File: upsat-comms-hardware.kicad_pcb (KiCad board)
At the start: 4 copper layers, 92.5 x 92.5 mm, 290 parts, among them J1 SMA, J2 SMA, P1 SWD, P2 OBC, P3 CONN_02X03, U1 TXCO_TG_5021CG, U10 CC1120, U12 ADT7420, U14 OPA320, U16 RF5110G, U18 FA_128_, U2 TPS79930, U3 FA_128_, U4 CC1120, U5 STM32F407VG, U6 TXCO_TG_5021CG, U8 TPS79930, Y1 Crystal, Y2 Crystal

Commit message: Restructuring libraries.
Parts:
- moved R72 0.05 mm to (132.4, 102.0)
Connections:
- P2 pad 6: Net-(P2-Pad6) -> (no net)
- U1 pad 1: Net-(U1-Pad1) -> (no net)
- U10 pad 16: Net-(U10-Pad16) -> (no net)
- U12 pad 10: Net-(U12-Pad10) -> (no net)
- U12 pad 13: Net-(U12-Pad13) -> (no net)
- U12 pad 14: Net-(U12-Pad14) -> (no net)
- U12 pad 15: Net-(U12-Pad15) -> (no net)
- U12 pad 16: Net-(U12-Pad16) -> (no net)
- U12 pad 5: Net-(U12-Pad5) -> (no net)
- U12 pad 6: Net-(U12-Pad6) -> (no net)
- U12 pad 7: Net-(U12-Pad7) -> (no net)
- U12 pad 8: Net-(U12-Pad8) -> (no net)
- U12 pad 9: Net-(U12-Pad9) -> (no net)
- U16 pad 13: Net-(U16-Pad13) -> (no net)
- U16 pad 7: Net-(U16-Pad7) -> (no net)
- U4 pad 16: Net-(U4-Pad16) -> (no net)
- U5 pad 1: Net-(U5-Pad1) -> (no net)
- U5 pad 15: Net-(U5-Pad15) -> (no net)
- U5 pad 16: Net-(U5-Pad16) -> (no net)
- U5 pad 17: Net-(U5-Pad17) -> (no net)
- U5 pad 18: Net-(U5-Pad18) -> (no net)
- U5 pad 2: Net-(U5-Pad2) -> (no net)
- U5 pad 23: Net-(U5-Pad23) -> (no net)
- U5 pad 24: Net-(U5-Pad24) -> (no net)
- U5 pad 29: Net-(U5-Pad29) -> (no net)
- U5 pad 3: Net-(U5-Pad3) -> (no net)
- U5 pad 33: Net-(U5-Pad33) -> (no net)
- U5 pad 34: Net-(U5-Pad34) -> (no net)
- U5 pad 35: Net-(U5-Pad35) -> (no net)
- U5 pad 37: Net-(U5-Pad37) -> (no net)
- U5 pad 39: Net-(U5-Pad39) -> (no net)
- U5 pad 4: Net-(U5-Pad4) -> (no net)
- U5 pad 41: Net-(U5-Pad41) -> (no net)
- U5 pad 42: Net-(U5-Pad42) -> (no net)
- U5 pad 43: Net-(U5-Pad43) -> (no net)
- U5 pad 44: Net-(U5-Pad44) -> (no net)
- U5 pad 45: Net-(U5-Pad45) -> (no net)
- U5 pad 5: Net-(U5-Pad5) -> (no net)
- U5 pad 55: Net-(U5-Pad55) -> (no net)
- U5 pad 56: Net-(U5-Pad56) -> (no net)
- U5 pad 57: Net-(U5-Pad57) -> (no net)
- U5 pad 58: Net-(U5-Pad58) -> (no net)
- U5 pad 59: Net-(U5-Pad59) -> (no net)
- U5 pad 60: Net-(U5-Pad60) -> (no net)
- U5 pad 61: Net-(U5-Pad61) -> (no net)
- U5 pad 62: Net-(U5-Pad62) -> (no net)
- U5 pad 63: Net-(U5-Pad63) -> (no net)
- U5 pad 64: Net-(U5-Pad64) -> (no net)
- U5 pad 65: Net-(U5-Pad65) -> (no net)
- U5 pad 66: Net-(U5-Pad66) -> (no net)
- U5 pad 68: Net-(U5-Pad68) -> (no net)
- U5 pad 7: Net-(U5-Pad7) -> (no net)
- U5 pad 70: Net-(U5-Pad70) -> (no net)
- U5 pad 71: Net-(U5-Pad71) -> (no net)
- U5 pad 78: Net-(U5-Pad78) -> (no net)
- U5 pad 79: Net-(U5-Pad79) -> (no net)
- U5 pad 81: Net-(U5-Pad81) -> (no net)
- U5 pad 82: Net-(U5-Pad82) -> (no net)
- U5 pad 85: Net-(U5-Pad85) -> (no net)
- U5 pad 86: Net-(U5-Pad86) -> (no net)
- U5 pad 87: Net-(U5-Pad87) -> (no net)
- U5 pad 88: Net-(U5-Pad88) -> (no net)
- U5 pad 90: Net-(U5-Pad90) -> (no net)
- U5 pad 91: Net-(U5-Pad91) -> (no net)
- U5 pad 92: Net-(U5-Pad92) -> (no net)
- U5 pad 93: Net-(U5-Pad93) -> (no net)
- U5 pad 97: Net-(U5-Pad97) -> (no net)
- U5 pad 98: Net-(U5-Pad98) -> (no net)
- U6 pad 1: Net-(U6-Pad1) -> (no net)
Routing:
- net Net-(R72-Pad2): track 29.2 -> 24.5 mm
- net Net-(R73-Pad2): track 30.0 -> 26.3 mm
- net /I2C1_SDA: track 150.8 -> 149.4 mm
- net /I2C1_SCL: track 153.8 -> 152.7 mm
- net /DAC_OUT2: track 100.0 -> 98.9 mm
- net Net-(R70-Pad2): track 22.3 -> 22.9 mm

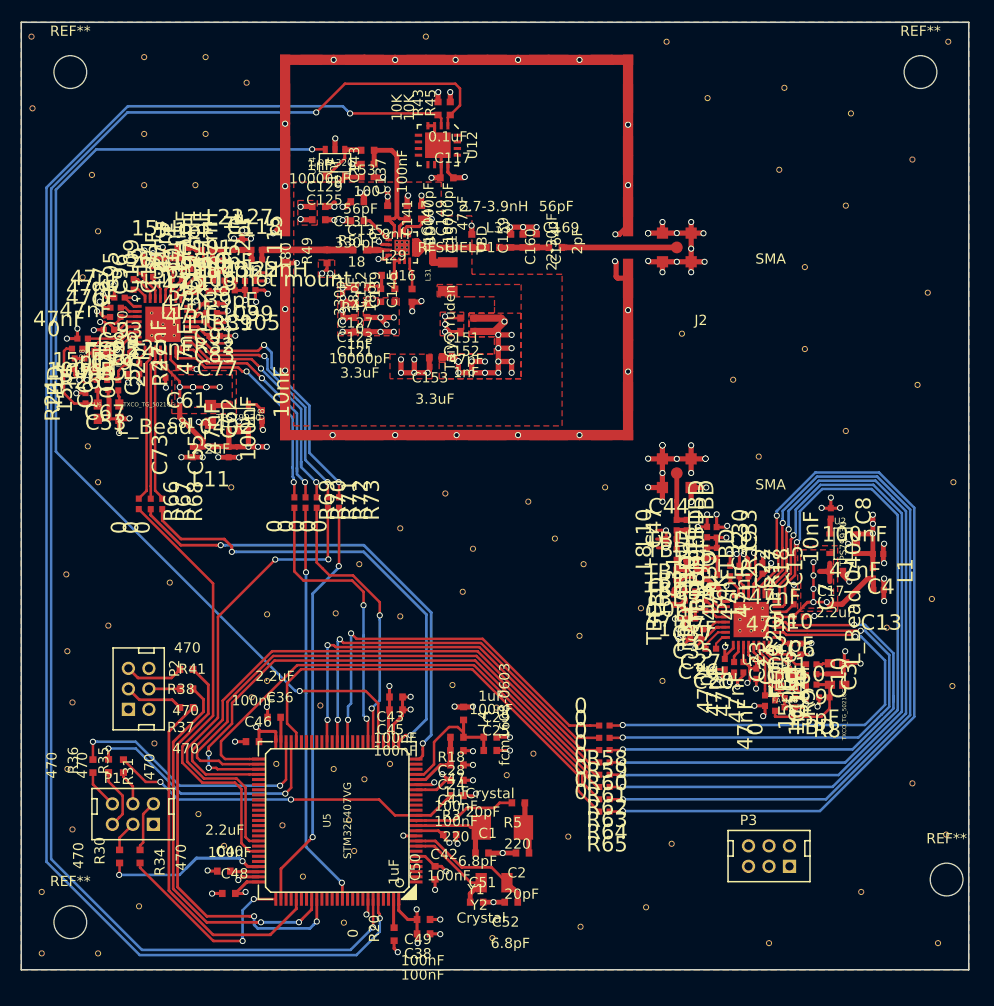
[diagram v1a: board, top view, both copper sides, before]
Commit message: Create silkscreen and reroute OBC Connector.
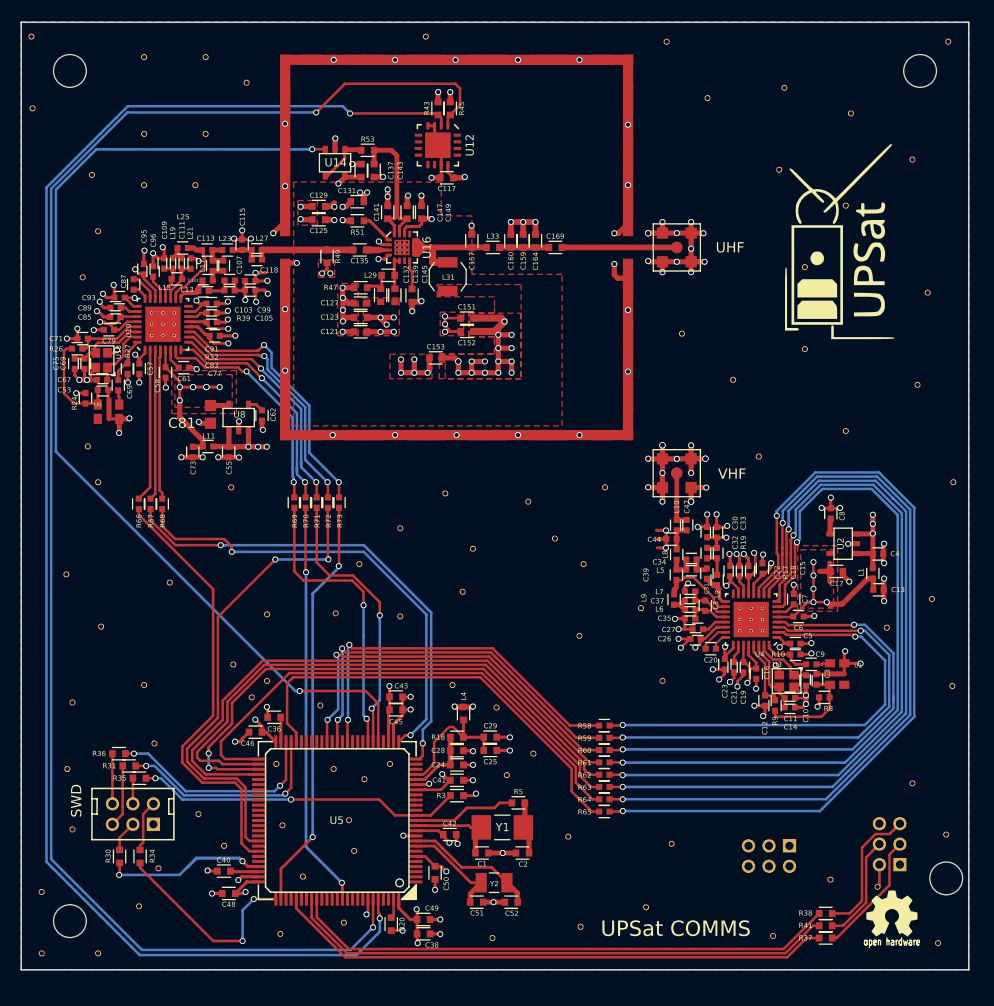
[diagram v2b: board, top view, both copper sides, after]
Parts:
- added G***: LOGO, libs:upsat-logo, F.Cu at (182.4, 76.0)
- added G***: LOGO, w_logo:Logo_silk_OSHW_6x6mm, F.Cu at (187.5, 141.6)
- added REF**: VIA-0.6mm, via:VIA-0.6mm, F.Cu at (127.8, 143.6)
- added REF**: VIA-0.6mm, via:VIA-0.6mm, F.Cu at (181.5, 138.3)
- added REF**: VIA-0.6mm, via:VIA-0.6mm, F.Cu at (123.2, 117.3)
- added REF**: VIA-0.6mm, via:VIA-0.6mm, F.Cu at (115.9, 137.2)
- EPS: renamed from P3; moved to B.Cu
- OBC: renamed from P2; moved to B.Cu
- RFSHIELD1: footprint libs:BMI-S-x06 -> BMI-S-x06:BMI-S-x06
- U18, U3: footprint w_crystal:crystal_fa128 -> libs:crystal_fa128
- UHF: renamed from J2; footprint libs:sma_smd_samtec_man -> comms_upsat:mmcx_conn
- VHF: renamed from J1; footprint libs:sma_smd_samtec_man -> comms_upsat:mmcx_conn
- moved OBC 74.9 mm to (187.3, 134.8)
- moved R38 68.0 mm to (181.7, 141.6), turned to 180 degrees
- moved R37 67.5 mm to (181.7, 144.0), turned to 180 degrees
- moved R41 65.4 mm to (180.4, 142.8), turned to 0 degrees
- moved REF** 6.77 mm to (114.5, 119.3)
- moved REF** 4.08 mm to (110.3, 113.6)
- moved R36 3.22 mm to (112.7, 126.0), turned to 180 degrees
- moved R35 2.85 mm to (114.7, 128.4), turned to 180 degrees
- moved REF** 1.68 mm to (186.1, 139.0)
- moved R31 1.52 mm to (112.4, 127.2), turned to 0 degrees
- moved R20 1.02 mm to (138.6, 142.0)
- moved C46 0.97 mm to (126.0, 123.9)
- moved REF** 0.81 mm to (175.9, 143.8)
- moved REF** 0.12 mm to (107.2, 142.3)
- moved REF** 0.12 mm to (107.2, 59.4)
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- renumbered P1 to SWD
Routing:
- net /COMMS_TO_OBC_TX: track 35.1 -> 54.7 mm
- net /COMMS_TO_OBC_RX: track 37.6 -> 53.9 mm, vias 2 -> 0
- net /COMMS_TO_OBC_EN: track 41.3 -> 53.5 mm, vias 2 -> 0
- net Net-(P2-Pad5): track 5.77 -> 13.3 mm
- net Net-(P2-Pad4): track 3.04 -> 10.5 mm
- net Net-(P2-Pad3): track 5.79 -> 12.2 mm
- net /USART3_RX: track 26.3 -> 21.4 mm
- net /USART3_TX: track 25.4 -> 21.2 mm
- net /NRST: track 35.0 -> 32.0 mm
- net GND: track 349.7 -> 351.8 mm
- net +3V3: track 103.6 -> 101.8 mm
- net /2GPIO2: track 40.2 -> 38.5 mm
- net /2RESET_N: track 38.7 -> 37.3 mm
- net /2GPIO3: track 39.4 -> 38.1 mm
- net Net-(P1-Pad6): track 3.84 -> 4.90 mm
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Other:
- board text added: "In memory of K. Efstathiou"
- board text added: "UPSat COMMS"

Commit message: Add vias on PA.
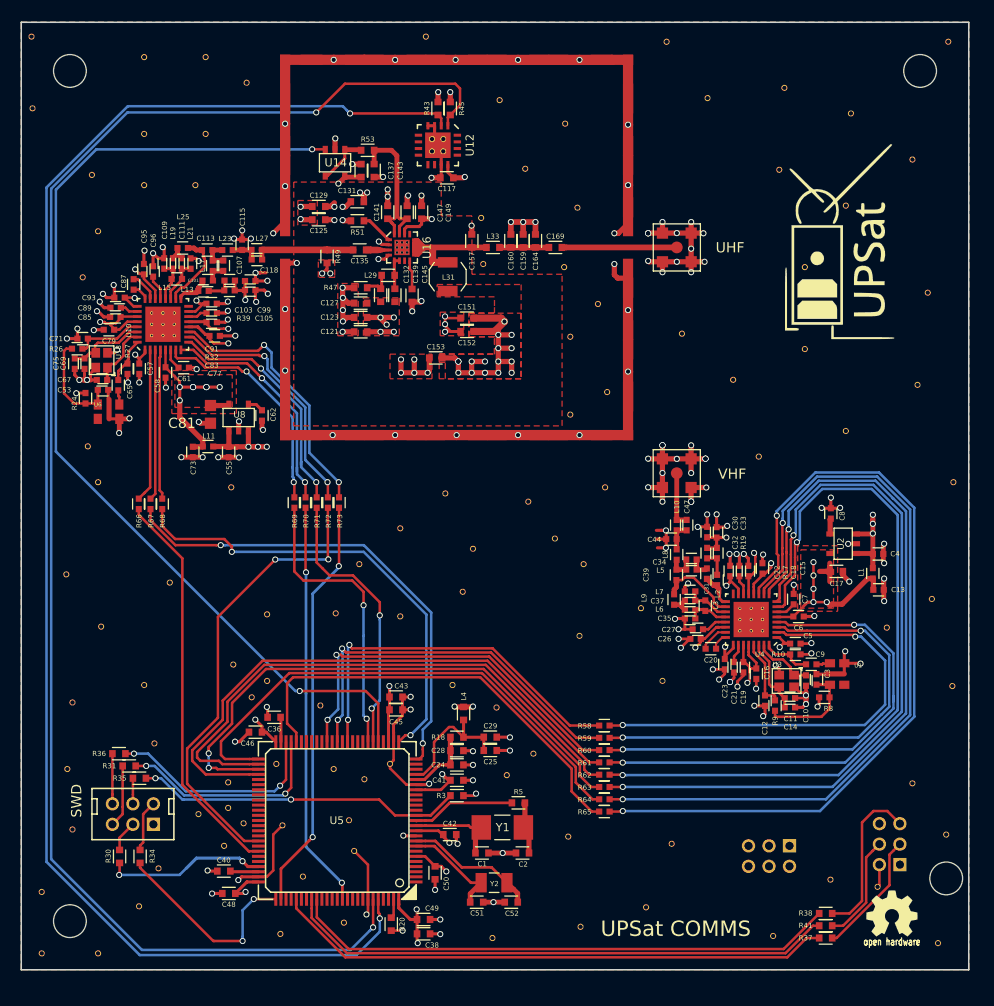
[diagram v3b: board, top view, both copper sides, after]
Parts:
- added REF**: VIA-0.6mm, via:VIA-0.6mm, F.Cu at (158.8, 82.1)
- added REF**: VIA-0.6mm, via:VIA-0.6mm, F.Cu at (151.7, 68.9)
- added REF**: VIA-0.6mm, via:VIA-0.6mm, F.Cu at (149.2, 62.2)
- added REF**: VIA-0.6mm, via:VIA-0.6mm, F.Cu at (122.7, 128.8)
- added REF**: VIA-0.6mm, via:VIA-0.6mm, F.Cu at (124.2, 132.8)
- added REF**: VIA-0.6mm, via:VIA-0.6mm, F.Cu at (122.7, 131.3)
- added REF**: VIA-0.6mm, via:VIA-0.6mm, F.Cu at (142.6, 67.2)
- added REF**: VIA-0.6mm, via:VIA-0.6mm, F.Cu at (143.7, 67.2)
- added REF**: VIA-0.6mm, via:VIA-0.6mm, F.Cu at (143.7, 66.0)
- added REF**: VIA-0.6mm, via:VIA-0.6mm, F.Cu at (142.6, 66.0)
- added REF**: VIA-0.6mm, via:VIA-0.6mm, F.Cu at (159.7, 90.7)
- added REF**: VIA-0.6mm, via:VIA-0.6mm, F.Cu at (156.1, 92.9)
- added REF**: VIA-0.6mm, via:VIA-0.6mm, F.Cu at (156.1, 85.3)
- added REF**: VIA-0.6mm, via:VIA-0.6mm, F.Cu at (155.5, 78.5)
- added REF**: VIA-0.6mm, via:VIA-0.6mm, F.Cu at (147.6, 78.2)
- added REF**: VIA-0.6mm, via:VIA-0.6mm, F.Cu at (147.4, 73.7)
- added REF**: VIA-0.6mm, via:VIA-0.6mm, F.Cu at (156.8, 72.7)
- added REF**: VIA-0.6mm, via:VIA-0.6mm, F.Cu at (155.6, 64.5)
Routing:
- net GND: track 351.8 -> 369.4 mm
- net /1RESET_N: track 43.1 -> 38.8 mm
- net Net-(P2-Pad5): track 13.3 -> 15.7 mm
- net /1GPIO0: track 46.6 -> 45.0 mm
